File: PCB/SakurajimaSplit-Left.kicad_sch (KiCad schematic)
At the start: 48 parts, among them J1 SWD, J10 Conn_01x01_Pin, J11 Conn_01x01_Pin, J12 Conn_01x01_Pin, J13 Conn_01x01_Pin, J14 Conn_01x01_Pin, J2 USB-C to Right-Half, J3 Conn_01x01_Pin, J32 Conn_01x01_Pin, J33 Conn_01x01_Pin, J34 Conn_01x01_Pin, J4 Conn_01x01_Pin, J5 Conn_01x01_Pin, J6 Conn_01x01_Pin, J7 Conn_01x01_Pin, J8 Conn_01x01_Pin, J9 Conn_01x01_Pin, SW1 SWCLK/BOOT0, U1 USBLC6-2SC6, U10 ZJY_M233, U2 STM32G0B1CBT6, U3 W25Q128JVS, Y1 8MHz

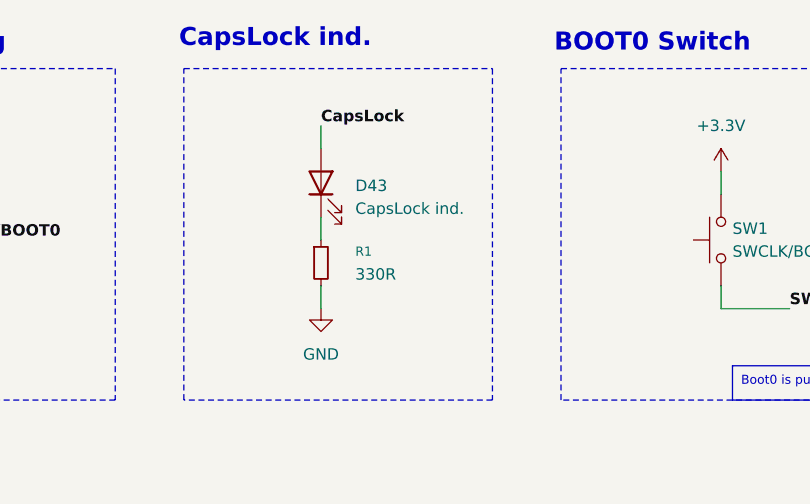
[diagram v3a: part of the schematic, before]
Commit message: fix(sch): swap LEDs with their series resistors
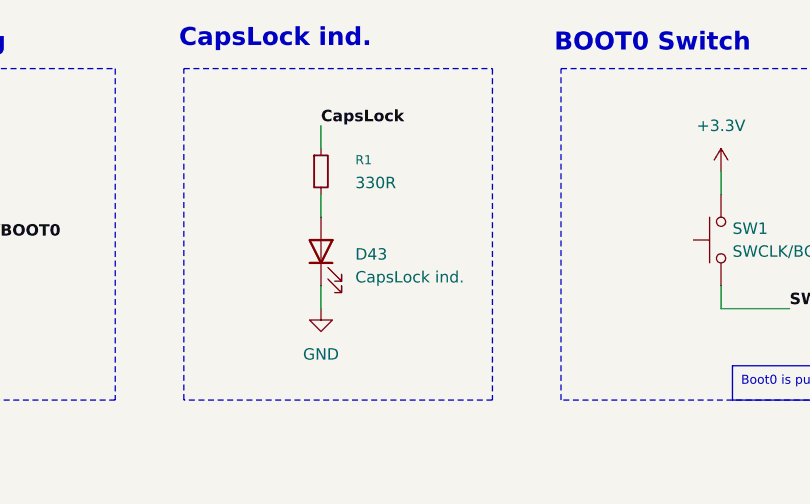
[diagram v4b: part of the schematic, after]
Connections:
- net CapsLock: now also R1.1; no longer D43.2 (A)
- net GND: now also D43.1 (K); no longer R1.2
- new net: D43.2 (A), R1.2
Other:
- moved on the sheet: D43, R1
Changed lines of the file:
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@@
 	(wire
 		(pts
+			(xy 87.63 41.91) (xy 87.63 44.45)
+		)
+		(stroke
+			(width 0)
+			(type default)
+		)
+	)
+	(wire
+		(pts
 			(xy 237.49 170.18) (xy 240.03 170.18)
 		)
@@
 	(wire
 		(pts
-			(xy 87.63 44.45) (xy 87.63 46.99)
-		)
-		(stroke
-			(width 0)
-			(type default)
-		)
-	)
-	(wire
-		(pts
 			(xy 237.49 180.34) (xy 240.03 180.34)
 		)
@@
 	(symbol
 		(lib_id "Device:LED")
-		(at 87.63 40.64 90)
+		(at 87.63 48.26 90)
 		(unit 1)
 		(exclude_from_sim no)
@@
 		(fields_autoplaced yes)
 		(property "Reference" "D43"
-			(at 91.44 40.9574 90)
+			(at 91.44 48.5774 90)
 			(effects
 				(font
@@
 		)
 		(property "Value" "CapsLock ind."
-			(at 91.44 43.4974 90)
+			(at 91.44 51.1174 90)
 			(effects
 				(font
@@
 		)
 		(property "Footprint" "LED_SMD:LED_0603_1608Metric"
-			(at 87.63 40.64 0)
+			(at 87.63 48.26 0)
 			(effects
 				(font
@@
 		)
 		(property "Datasheet" "~"
-			(at 87.63 40.64 0)
+			(at 87.63 48.26 0)
 			(effects
 				(font
@@
 		)
 		(property "Description" "Light emitting diode"
-			(at 87.63 40.64 0)
+			(at 87.63 48.26 0)
 			(effects
 				(font
@@
 		)
 		(property "Sim.Pins" "1=K 2=A"
-			(at 87.63 40.64 0)
+			(at 87.63 48.26 0)
 			(effects
 				(font
@@
 		)
 		(property "Distributor Link" "https://lionelectronic.ir/products/2215-XL-1608UWC-04"
-			(at 87.63 40.64 90)
+			(at 87.63 48.26 90)
 			(effects
 				(font
@@
 		)
 		(property "Manufacturer" "XINGLIGHT"
-			(at 87.63 40.64 90)
+			(at 87.63 48.26 90)
 			(effects
 				(font
@@
 		)
 		(property "Manufacturer Part No." "XL-1608UWC-04"
-			(at 87.63 40.64 90)
+			(at 87.63 48.26 90)
 			(effects
 				(font
@@
 	(symbol
 		(lib_id "Device:R_Small")
-		(at 87.63 49.53 0)
+		(at 87.63 39.37 0)
 		(unit 1)
 		(exclude_from_sim no)
@@
 		(fields_autoplaced yes)
 		(property "Reference" "R1"
-			(at 91.44 48.2599 0)
+			(at 91.44 38.0999 0)
 			(effects
 				(font
@@
 		)
 		(property "Value" "330R"
-			(at 91.44 50.7999 0)
+			(at 91.44 40.6399 0)
 			(effects
 				(font
@@
 		)
 		(property "Footprint" "Resistor_SMD:R_0603_1608Metric"
-			(at 87.63 49.53 0)
+			(at 87.63 39.37 0)
 			(effects
 				(font
@@
 		)
 		(property "Datasheet" "~"
-			(at 87.63 49.53 0)
+			(at 87.63 39.37 0)
 			(effects
 				(font
@@
 		)
 		(property "Description" "Resistor, small symbol"
-			(at 87.63 49.53 0)
+			(at 87.63 39.37 0)
 			(effects
 				(font
@@
 		)
 		(property "Distributor Link" "https://lionelectronic.ir/products/1182-SER0603F330R"
-			(at 87.63 49.53 0)
+			(at 87.63 39.37 0)
 			(effects
 				(font
@@
 		)
 		(property "Manufacturer" "VO Sub Brand (ER)"
-			(at 87.63 49.53 0)
+			(at 87.63 39.37 0)
 			(effects
 				(font
@@
 		)
 		(property "Manufacturer Part No." "SER0603F330R"
-			(at 87.63 49.53 0)
+			(at 87.63 39.37 0)
 			(effects
 				(font

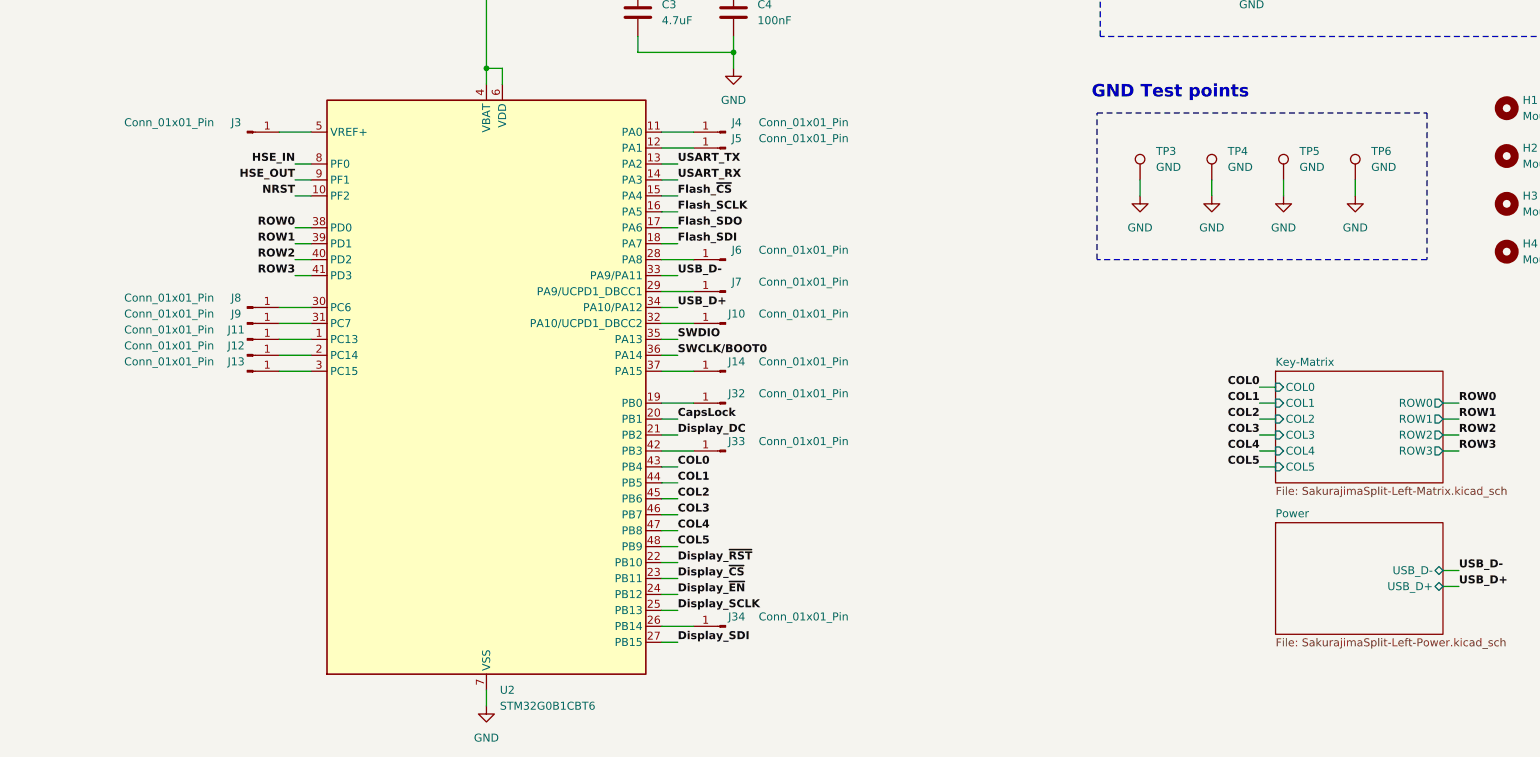
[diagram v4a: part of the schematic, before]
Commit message: feat(pcb): design rough layout and update schematic accordingly
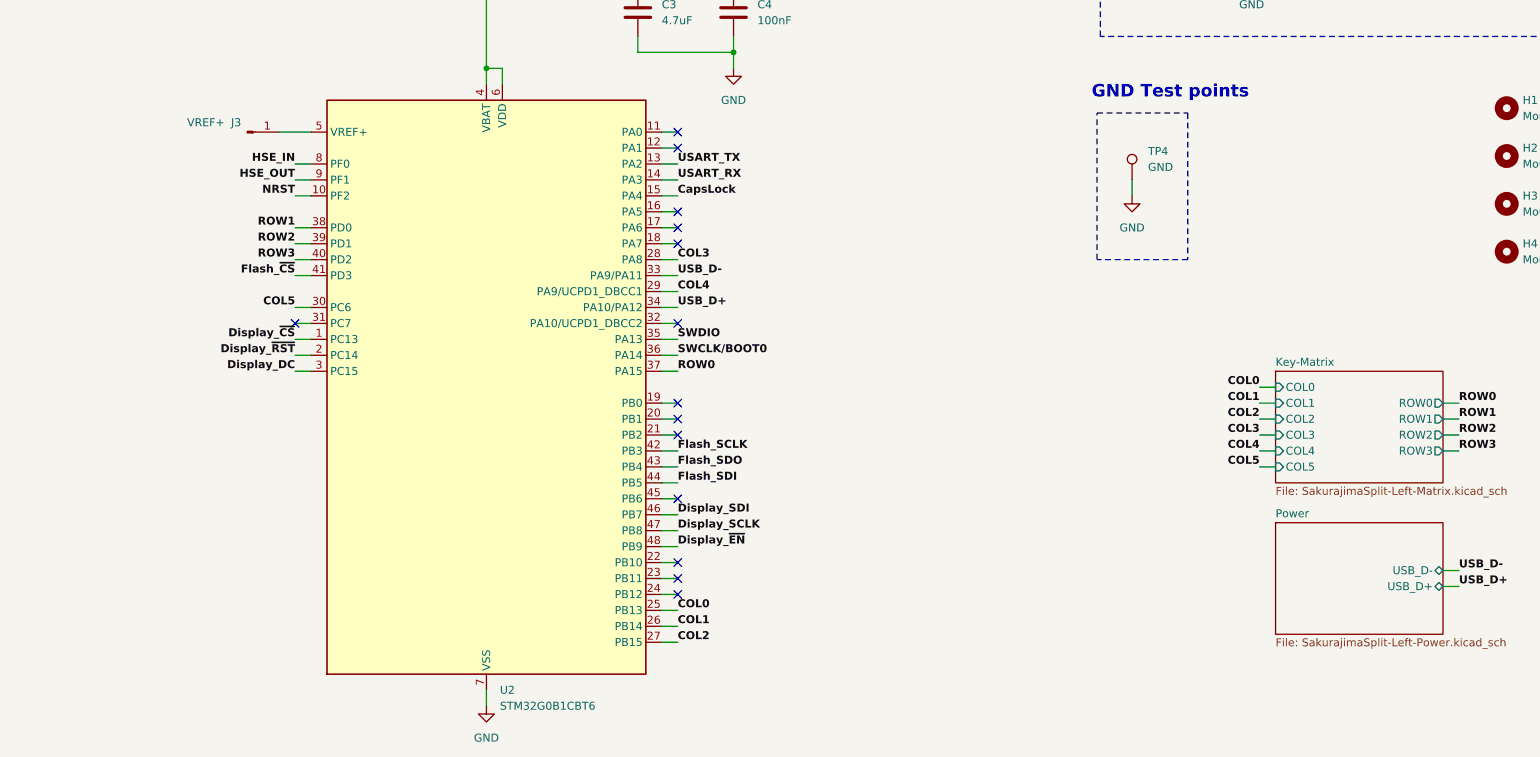
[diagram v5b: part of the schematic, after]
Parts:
- removed J10, J11, J12, J13, J14, J32, J33, J34, J4, J5, J6, J7, J8, J9: Conn_01x01_Pin, Connector_Wire:SolderWirePad_1x01_SMD_1x2mm, symbol Connector:Conn_01x01_Pin
- removed TP3, TP5, TP6: GND, Hayata_Lib:TestPoint_Pad_Circular_1.3mm, symbol Connector:TestPoint
- J3: value Conn_01x01_Pin -> VREF+
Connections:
- net COL0: now also U2.25 (PB13); no longer U2.43 (PB4)
- net COL1: now also U2.26 (PB14); no longer U2.44 (PB5)
- net COL2: now also U2.27 (PB15); no longer U2.45 (PB6)
- net COL3: now also U2.28 (PA8); no longer U2.46 (PB7)
- net COL4: now also U2.29 (PA9/UCPD1_DBCC1); no longer U2.47 (PB8)
- net COL5: now also U2.30 (PC6); no longer U2.48 (PB9)
- net CapsLock: now also U2.15 (PA4); no longer U2.20 (PB1)
- net Display_DC: now also U2.3 (PC15); no longer U2.21 (PB2)
- net Display_SCLK: now also U2.47 (PB8); no longer U2.25 (PB13)
- net Display_SDI: now also U2.46 (PB7); no longer U2.27 (PB15)
- net Display_~{CS}: now also U2.1 (PC13); no longer U2.23 (PB11)
- net Display_~{EN}: now also U2.48 (PB9); no longer U2.24 (PB12)
- net Display_~{RST}: now also U2.2 (PC14); no longer U2.22 (PB10)
- net Flash_SCLK: now also U2.42 (PB3); no longer U2.16 (PA5)
- net Flash_SDI: now also U2.44 (PB5); no longer U2.18 (PA7)
- net Flash_SDO: now also U2.43 (PB4); no longer U2.17 (PA6)
- net Flash_~{CS}: now also U2.41 (PD3); no longer U2.15 (PA4)
- net ROW0: now also U2.37 (PA15); no longer U2.38 (PD0)
- net ROW1: now also U2.38 (PD0); no longer U2.39 (PD1)
- net ROW2: now also U2.39 (PD1); no longer U2.40 (PD2)
- net ROW3: now also U2.40 (PD2); no longer U2.41 (PD3)
- no-connect marks 4 -> 18
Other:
- moved on the sheet: TP4

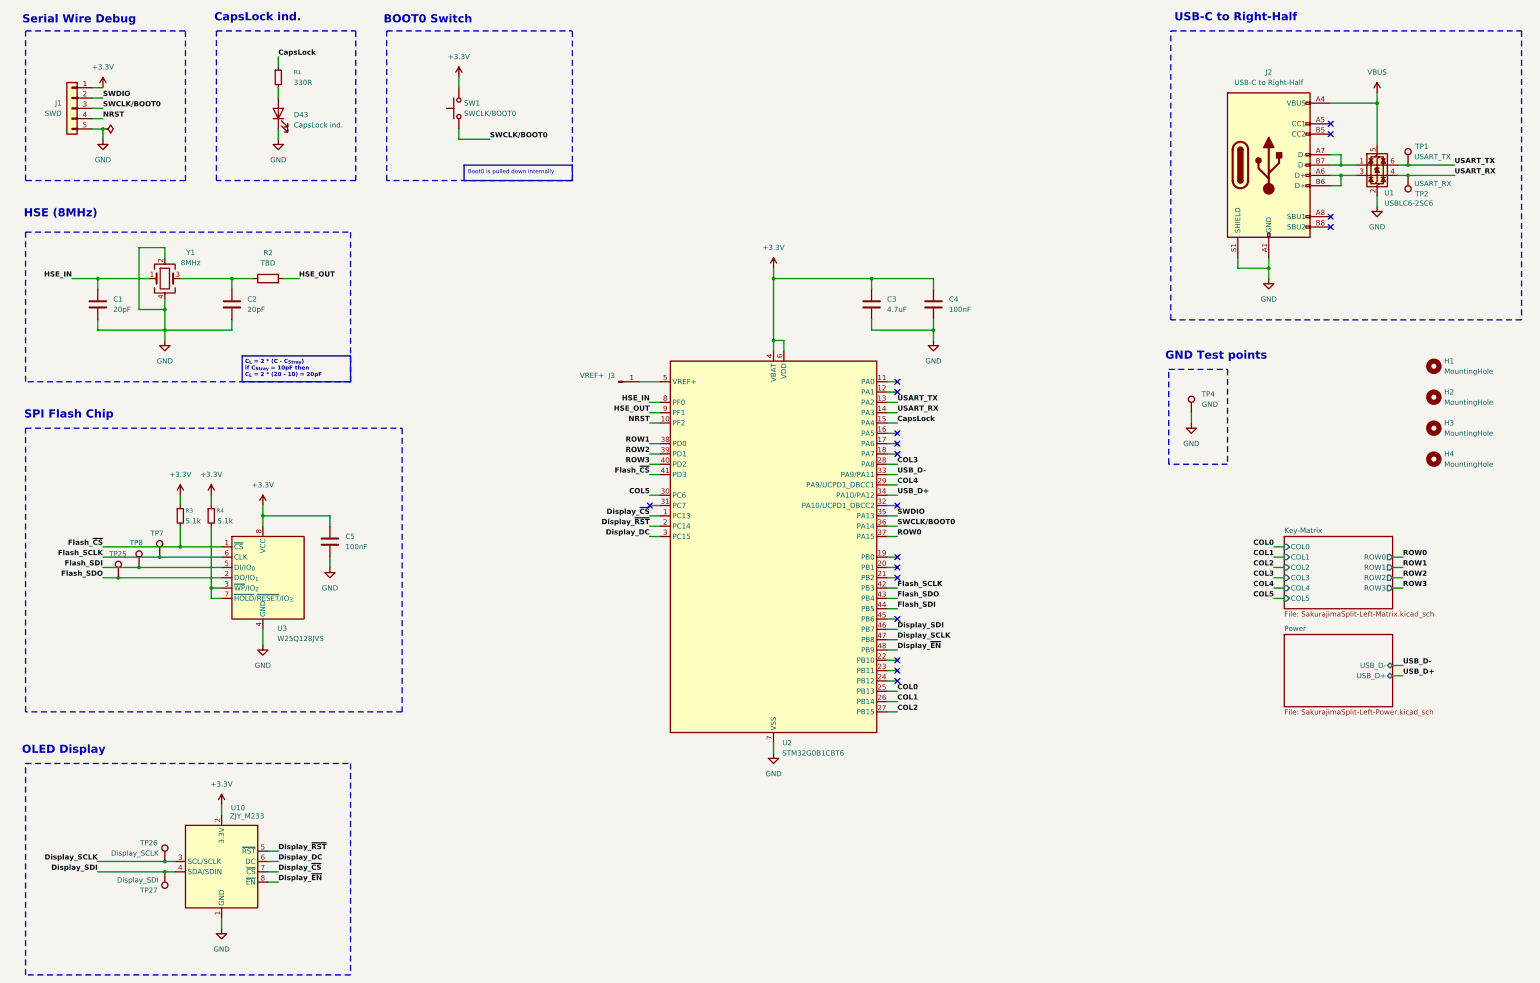
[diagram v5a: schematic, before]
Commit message: feat(pcb): finish designing rough layout and update schematic
- Removed unused MCU pads
- Removed some GND testpoints
- Updated MCU connections based on PCB layout and MCU orientation
- Updated key matrix layout for a less aggressive one which feels more
  comfortable and more visually pleasing
- Re-annotated schematic
- Finished rough component placement
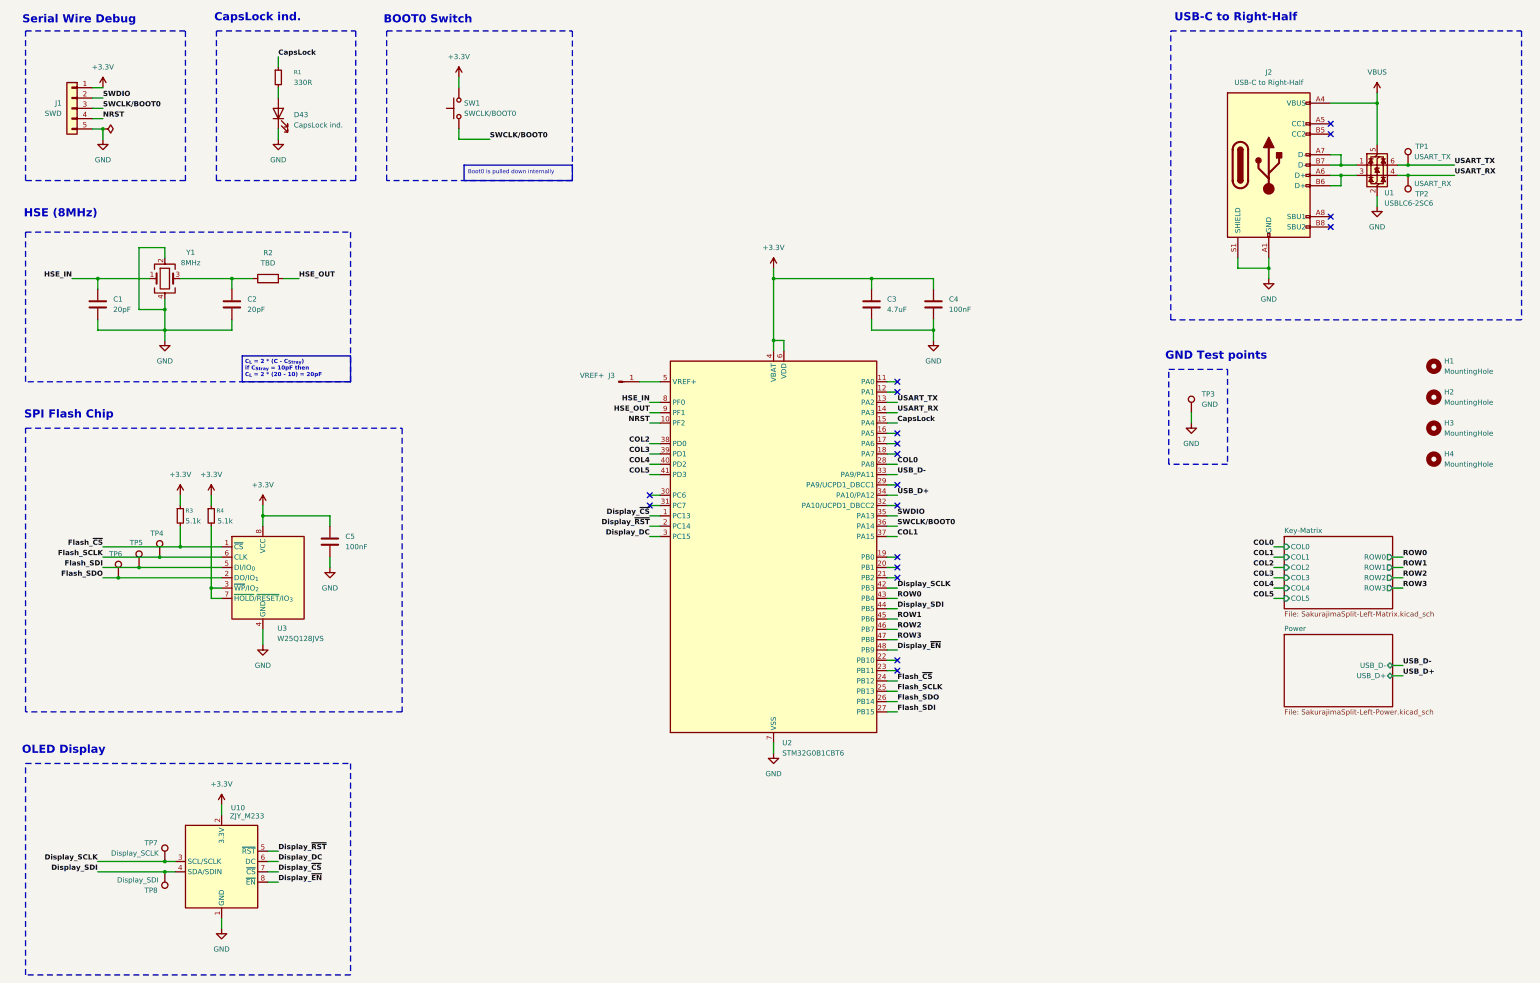
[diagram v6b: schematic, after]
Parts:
- renumbered TP4 to TP3, TP7 to TP4, TP8 to TP5, TP25 to TP6, TP26 to TP7, TP27 to TP8
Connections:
- net COL0: now also U2.28 (PA8); no longer U2.25 (PB13)
- net COL1: now also U2.37 (PA15); no longer U2.26 (PB14)
- net COL2: now also U2.38 (PD0); no longer U2.27 (PB15)
- net COL3: now also U2.39 (PD1); no longer U2.28 (PA8)
- net COL4: now also U2.40 (PD2); no longer U2.29 (PA9/UCPD1_DBCC1)
- net COL5: now also U2.41 (PD3); no longer U2.30 (PC6)
- net Display_SCLK: now also U2.42 (PB3); no longer U2.47 (PB8)
- net Display_SDI: now also U2.44 (PB5); no longer U2.46 (PB7)
- net Flash_SCLK: now also U2.25 (PB13); no longer U2.42 (PB3)
- net Flash_SDI: now also U2.27 (PB15); no longer U2.44 (PB5)
- net Flash_SDO: now also U2.26 (PB14); no longer U2.43 (PB4)
- net Flash_~{CS}: now also U2.24 (PB12); no longer U2.41 (PD3)
- net ROW0: now also U2.43 (PB4); no longer U2.37 (PA15)
- net ROW1: now also U2.45 (PB6); no longer U2.38 (PD0)
- net ROW2: now also U2.46 (PB7); no longer U2.39 (PD1)
- net ROW3: now also U2.47 (PB8); no longer U2.40 (PD2)
